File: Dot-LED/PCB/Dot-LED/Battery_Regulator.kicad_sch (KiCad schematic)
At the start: 1 part, among them U2 MCP73831-2-OT

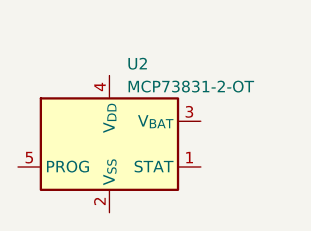
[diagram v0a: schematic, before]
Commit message: add common KiCad library using plugin
https://componentsearchengine.com/ga/downloads.php
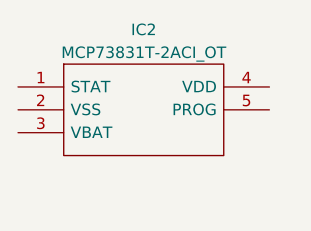
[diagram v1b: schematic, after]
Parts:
- removed U2: MCP73831-2-OT, Package_TO_SOT_SMD:SOT-23-5, symbol Battery_Management:MCP73831-2-OT
- added IC2: MCP73831T-2ACI_OT, SOT95P270X145-5N, symbol SamacSys_Parts:MCP73831T-2ACI_OT
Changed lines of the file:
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@@
 (kicad_sch (version 20230121) (generator eeschema)
   (paper "A4")
-  (symbol (lib_id "Battery_Management:MCP73831-2-OT") (at 139.7 82.55 0) (unit 1)
+  (symbol (lib_id "SamacSys_Parts:MCP73831T-2ACI_OT") (at 129.54 76.2 0) (unit 1)
     (in_bom yes) (on_board yes) (dnp no) (fields_autoplaced)
-    (property "Reference" "U2" (at 141.6559 73.66 0)
-      (effects (font (size 1.27 1.27)) (justify left))
+    (property "Reference" "IC2" (at 143.51 69.85 0)
+      (effects (font (size 1.27 1.27)))
     )
-    (property "Value" "MCP73831-2-OT" (at 141.6559 76.2 0)
-      (effects (font (size 1.27 1.27)) (justify left))
+    (property "Value" "MCP73831T-2ACI_OT" (at 143.51 72.39 0)
+      (effects (font (size 1.27 1.27)))
     )
-    (property "Footprint" "Package_TO_SOT_SMD:SOT-23-5" (at 140.97 88.9 0)
-      (effects (font (size 1.27 1.27) italic) (justify left) hide)
+    (property "Footprint" "SOT95P270X145-5N" (at 153.67 73.66 0)
+      (effects (font (size 1.27 1.27)) (justify left) hide)
     )
-    (property "Datasheet" "http://ww1.microchip.com/downloads/en/DeviceDoc/20001984g.pdf" (at 135.89 83.82 0)
-      (effects (font (size 1.27 1.27)) hide)
+    (property "Datasheet" "http://ww1.microchip.com/downloads/en/DeviceDoc/20001984g.pdf" (at 153.67 76.2 0)
+      (effects (font (size 1.27 1.27)) (justify left) hide)
+    )
+    (property "Description" "Li-Ion Charge Controller 4.2V SOT23-5" (at 153.67 78.74 0)
+      (effects (font (size 1.27 1.27)) (justify left) hide)
+    )
+    (property "Height" "1.45" (at 153.67 81.28 0)
+      (effects (font (size 1.27 1.27)) (justify left) hide)
+    )
+    (property "Manufacturer_Name" "Microchip" (at 153.67 83.82 0)
+      (effects (font (size 1.27 1.27)) (justify left) hide)
+    )
+    (property "Manufacturer_Part_Number" "MCP73831T-2ACI/OT" (at 153.67 86.36 0)
+      (effects (font (size 1.27 1.27)) (justify left) hide)
+    )
+    (property "Mouser Part Number" "579-MCP73831T-2ACIOT" (at 153.67 88.9 0)
+      (effects (font (size 1.27 1.27)) (justify left) hide)
+    )
+    (property "Mouser Price/Stock" "https://www.mouser.co.uk/ProductDetail/Microchip-Technology/MCP73831T-2ACI-OT?qs=yUQqVecv4qvbBQBGbHx0Mw%3D%3D" (at 153.67 91.44 0)
+      (effects (font (size 1.27 1.27)) (justify left) hide)
+    )
+    (property "Arrow Part Number" "MCP73831T-2ACI/OT" (at 153.67 93.98 0)
+      (effects (font (size 1.27 1.27)) (justify left) hide)
+    )
+    (property "Arrow Price/Stock" "https://www.arrow.com/en/products/mcp73831t-2aciot/microchip-technology?region=nac" (at 153.67 96.52 0)
+      (effects (font (size 1.27 1.27)) (justify left) hide)
     )
     (pin "1")
@@
       (project "Dot-LED"
         (path "/e63e39d7-6ac0-4ffd-8aa3-1841a4541b55/bfacb344-8895-4232-9d46-a3aaa9a06434"
-          (reference "U2") (unit 1)
+          (reference "IC2") (unit 1)
         )
       )

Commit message: Update DotLED Schem
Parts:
- added C3: 1uF, Capacitor_SMD:C_0603_1608Metric_Pad1.08x0.95mm_HandSolder, symbol SamacSys_Parts:0402B102K500NT
- added C4: 100nf, Capacitor_SMD:C_0603_1608Metric_Pad1.08x0.95mm_HandSolder, symbol SamacSys_Parts:0402B102K500NT
- added D3: LED, LED_SMD:LED_0603_1608Metric_Pad1.05x0.95mm_HandSolder, symbol Device:LED
- added R3: 4.3k, RESC1608X55N, symbol SamacSys_Parts:RMCF0603ZT0R00
- added R3: 1.5k, RESC1608X55N, symbol SamacSys_Parts:RMCF0603ZT0R00
- added U1: 3034, 3034, symbol SamacSys_Parts:3034
- IC2: Digi-Key_PN (none) -> 579-MCP73831T-2ACIOT
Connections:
- net at IC2.1 (STAT): now also D3.1 (K)
- net GND: now reaches IC2.2 (VSS)
- net GND: now also C3.1, C4.1, R3.1, U1.3 (NEG._CONTACT_PAD_(GND))
- net VBAT: now reaches IC2.3 (VBAT)
- net VBAT: now also C3.2, C4.2, U1.1, U1.2
- net VDD_IN: now reaches IC2.4 (VDD)
- net VDD_IN: now also R3.2
- net at IC2.5 (PROG): now also R3.2
- new net: D3.2 (A), R3.1
